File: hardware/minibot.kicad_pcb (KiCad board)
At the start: 2 copper layers, 52 parts, among them J1 USB_OTG, J2 RESET, J3 CONN_01X18, J4 BAUD, J5 SWD, J6 CONN_02X07, SW1 BOOT, SW2 RESET, U1 LSM6DS3US, U2 TLV70233DBV, U3 RN41, U4 STM32F411CEUx, Y1 12MHz

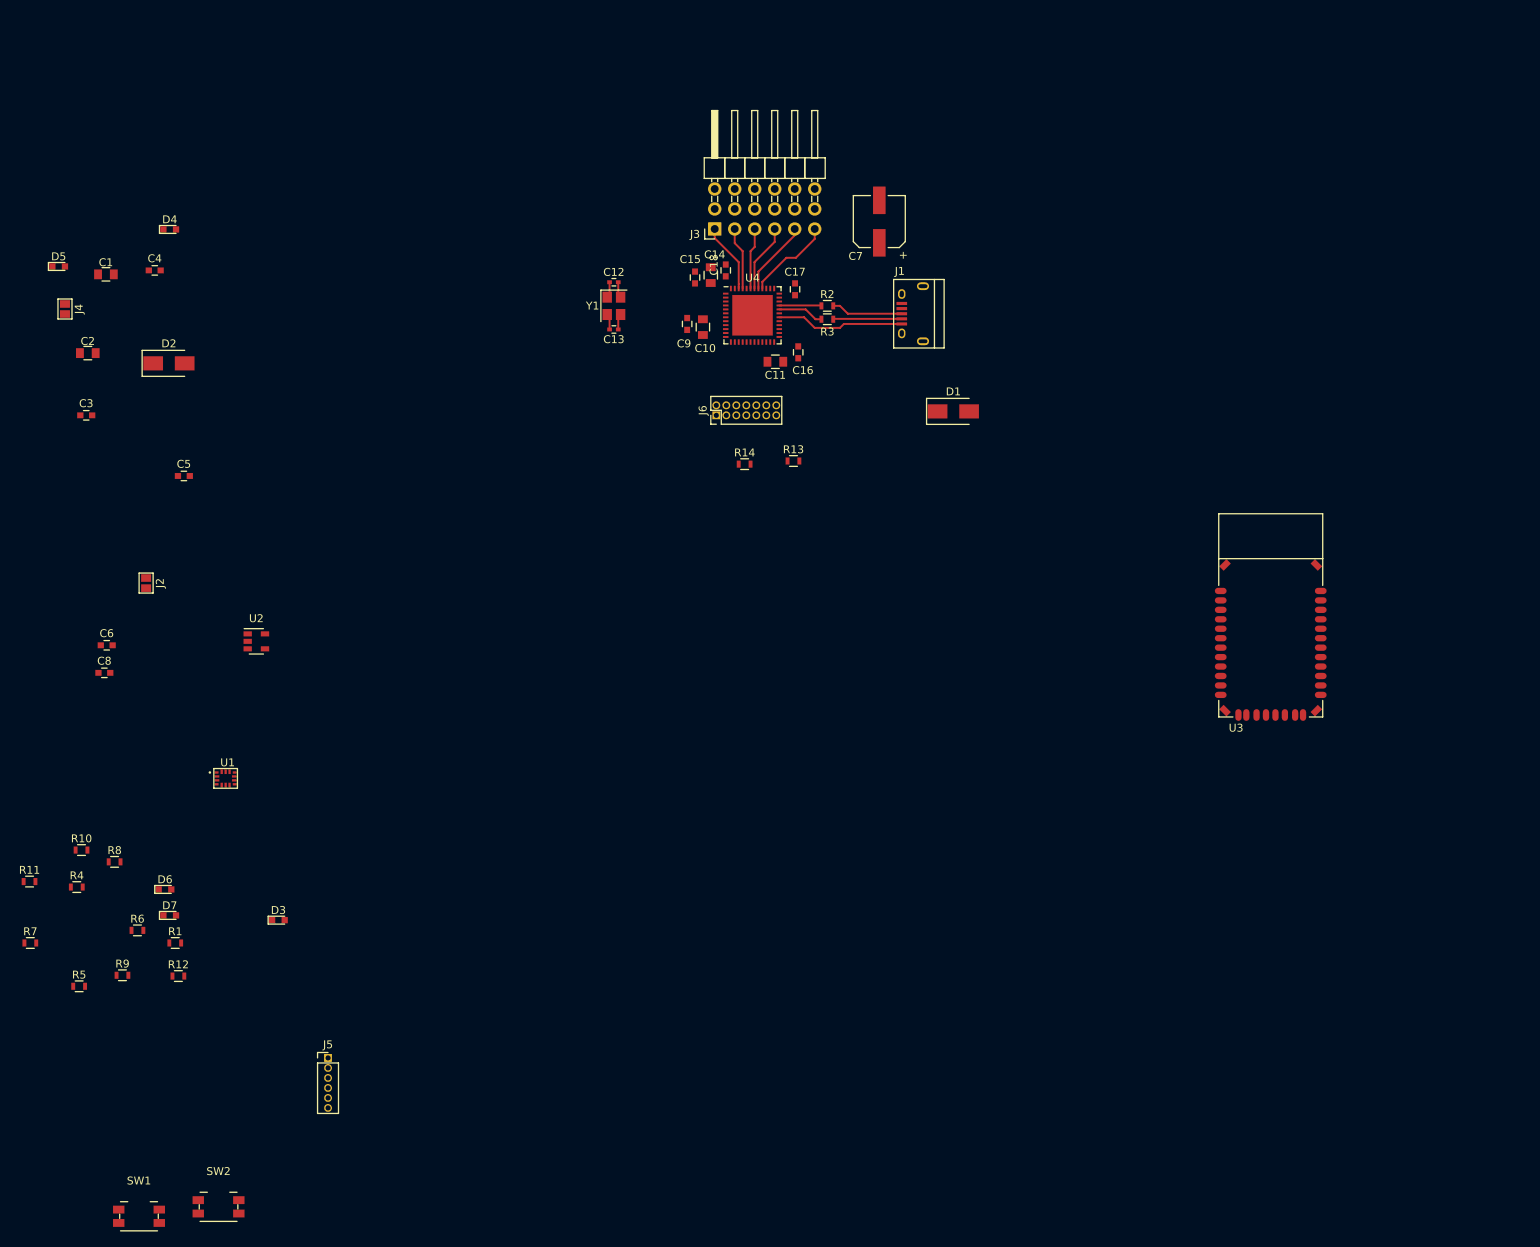
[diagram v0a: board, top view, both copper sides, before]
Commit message: Modify the schematic and PCB. At this stage the pinout should be considered and very careful selection of which peripheral goes where needs to be done.
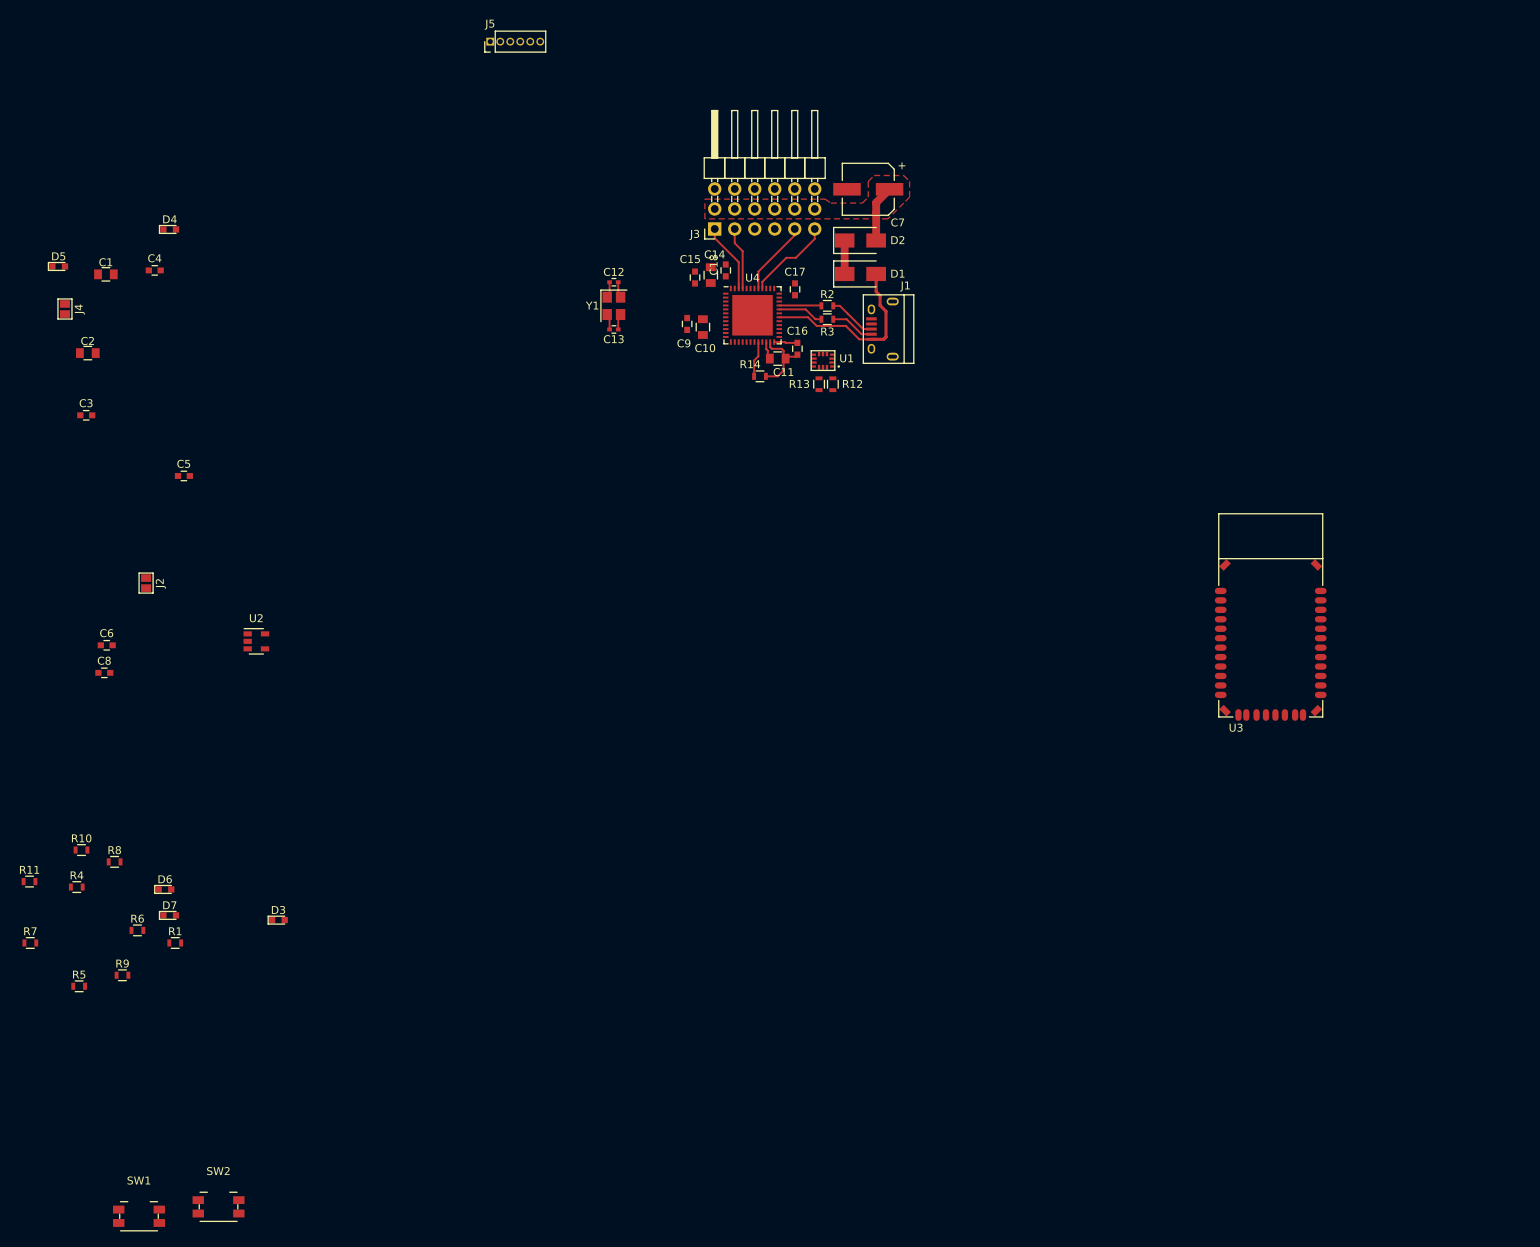
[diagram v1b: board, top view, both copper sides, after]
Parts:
- removed J6: CONN_02X07, Pin_Headers:Pin_Header_Straight_2x07_Pitch1.27mm
- moved J5 130.7 mm to (115.0, 19.8), turned to 90 degrees
- moved R12 112.0 mm to (158.5, 63.2), turned to 270 degrees
- moved U1 92.6 mm to (157.2, 60.2), turned to 180 degrees
- moved D2 89.2 mm to (162.0, 45.0)
- moved D1 21.1 mm to (162.0, 49.2)
- moved R14 11.3 mm to (149.2, 62.2)
- moved R13 10.3 mm to (156.8, 63.2), turned to 270 degrees
- moved C7 4.33 mm to (163.0, 38.5), turned to 180 degrees
- moved J1 4.32 mm to (164.8, 56.2)
- moved C11 0.50 mm to (151.5, 60.0)
- moved C16 0.46 mm to (154.0, 58.8)
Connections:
- C1 pad 2: (no net) -> Net-(C1-Pad2)
- J1 pad 4: (no net) -> Net-(J1-Pad4)
- R12 pad 1: /PB11 -> /PB7
- R13 pad 1: /PB10 -> /PB6
- U1 pad 10: (no net) -> Net-(U1-Pad10)
- U1 pad 13: /PB10 -> /PB6
- U1 pad 14: /PB11 -> /PB7
- U1 pad 4: (no net) -> Net-(U1-Pad4)
- U1 pad 9: (no net) -> Net-(U1-Pad9)
- U3 pad 11: (no net) -> VDD
- U4 pad 18: /PB0 -> /CH2
- U4 pad 19: /PB1 -> /CH3
- U4 pad 25: /PB11 -> /PB12
- U4 pad 26: /PB12 -> /PB13
- U4 pad 27: /PB13 -> /PB14
- U4 pad 28: /PB14 -> /PB15
- U4 pad 29: (no net) -> /PA8
- U4 pad 31: (no net) -> /PA10
- U4 pad 42: /CH2 -> /PB6
- U4 pad 43: /CH3 -> /PB7
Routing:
- net GND: track 4.05 -> 13.9 mm
- net /CH2: track 8.62 -> 0.00 mm
- net /CH3: track 7.78 -> 0.00 mm
- net Net-(C7-Pad1): track 0.00 -> 7.20 mm
- net /PA9: track 16.3 -> 23.4 mm
- net /PB2: track 0.00 -> 4.58 mm
- net +5V: track 0.00 -> 4.25 mm
- net Net-(J1-Pad3): track 9.11 -> 6.07 mm
- net Net-(J1-Pad2): track 8.72 -> 5.71 mm
- net +3V3: track 0.00 -> 2.99 mm
- net Net-(C11-Pad1): track 0.00 -> 2.18 mm
- added copper zone on F.Cu, net Net-(C7-Pad1)

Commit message: Redo the pinout. Plot the PDF. Layout the rest of the board.
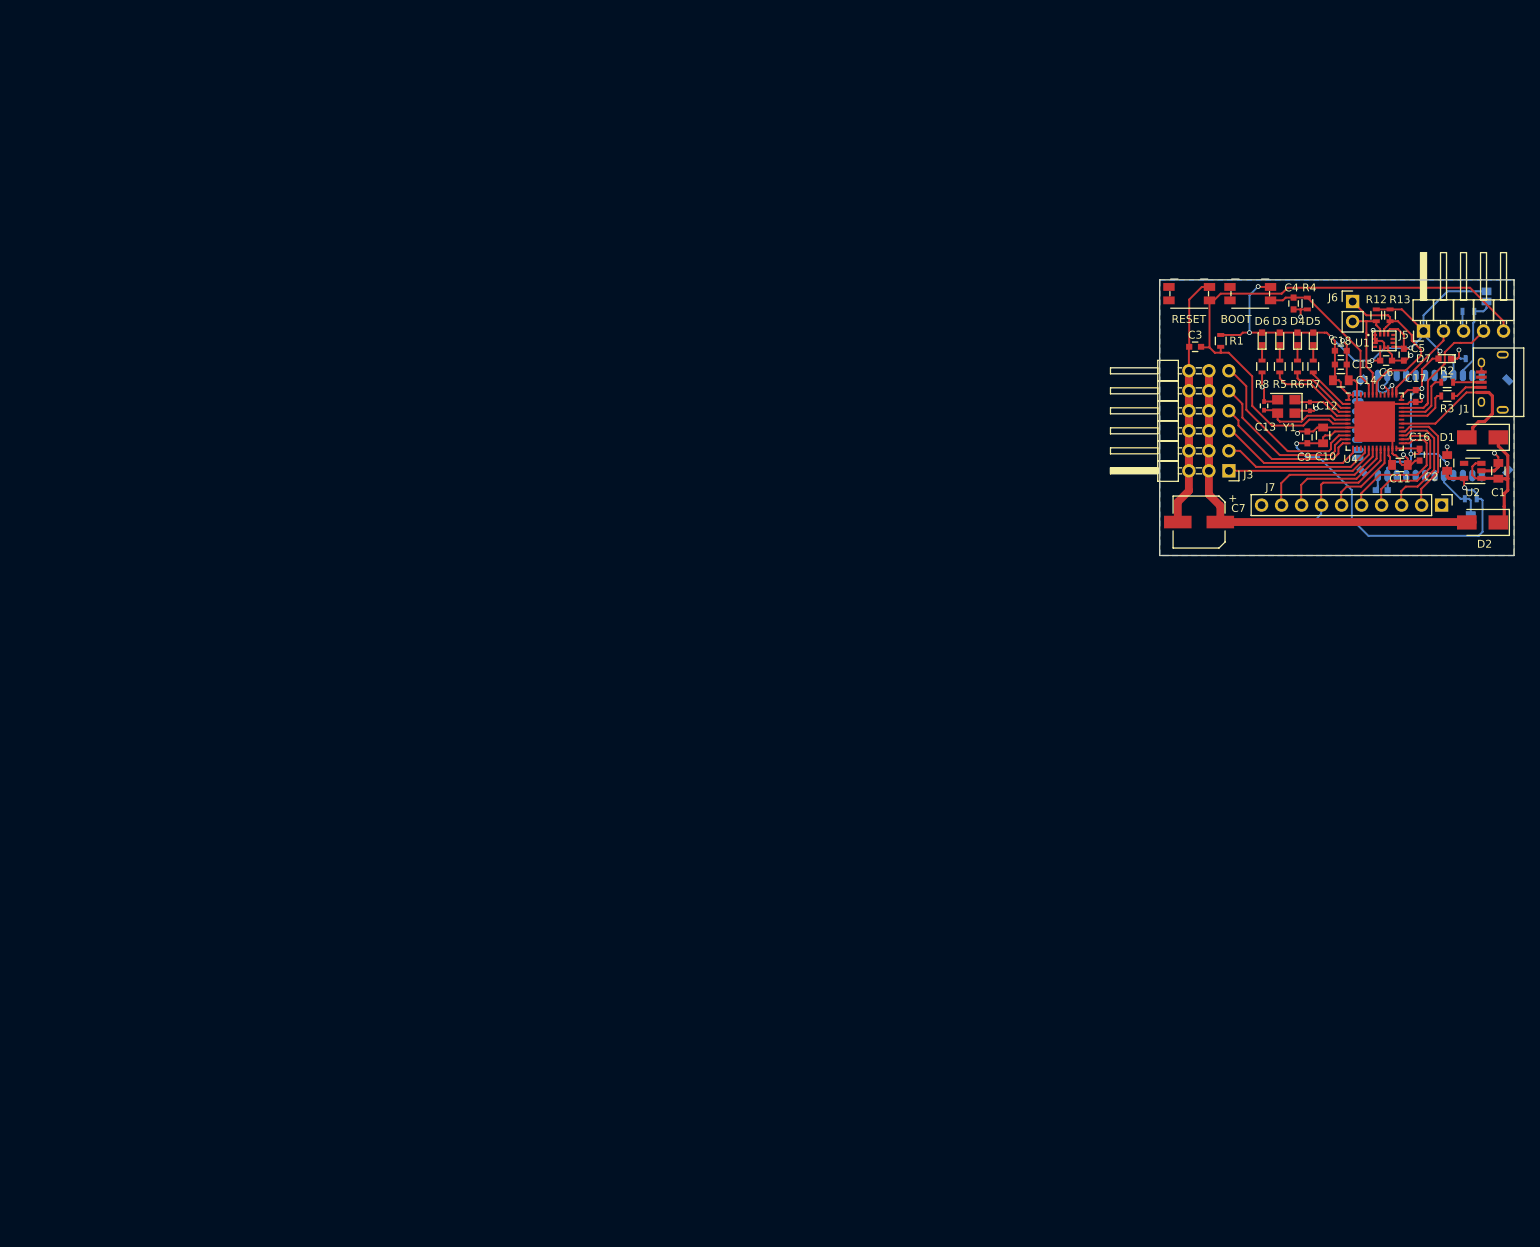
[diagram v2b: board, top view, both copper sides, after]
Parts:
- added J6: CONN_01X02, Pin_Headers:Pin_Header_Straight_1x02_Pitch2.54mm, F.Cu at (224.5, 52.8)
- added J7: CONN_01X10, Pin_Headers:Pin_Header_Straight_1x10_Pitch2.54mm, F.Cu at (235.8, 78.6)
- C8, J2, J4, R10, R11, R14, R9, U3: moved to B.Cu
- J5: value SWD -> CONN_01X05; footprint Pin_Headers:Pin_Header_Straight_1x06_Pitch1.27mm -> Pin_Headers:Pin_Header_Angled_1x05_Pitch2.54mm
- moved R11 196.5 mm to (239.2, 54.0)
- moved R10 185.8 mm to (238.1, 60.0)
- moved SW1 183.4 mm to (211.5, 51.8)
- moved R9 181.6 mm to (239.5, 77.8)
- moved J4 180.5 mm to (241.5, 52.1)
- moved R7 178.6 mm to (219.5, 61.0), turned to 90 degrees
- moved C1 178.6 mm to (243.0, 74.2), turned to 270 degrees
- moved D7 176.7 mm to (236.2, 60.0), turned to 180 degrees
- moved C2 173.2 mm to (236.5, 73.2), turned to 270 degrees
- moved R4 172.9 mm to (218.8, 53.0), turned to 270 degrees
- moved R5 171.6 mm to (215.2, 61.0), turned to 90 degrees
- moved SW2 169.2 mm to (203.8, 51.8)
- moved J2 168.4 mm to (239.5, 80.5), turned to 180 degrees
- moved C6 166.4 mm to (228.8, 60.2)
- moved C8 163.9 mm to (228.2, 76.7), turned to 180 degrees
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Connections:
- C1 pad 2: Net-(C1-Pad2) -> +5V
- SW2 pad 1: /nRST -> GND
- SW2 pad 2: GND -> /nRST
- U3 pad : (no net) -> GND
- U3 pad 11: VDD -> +3V3
- U3 pad 15: /BT_CTS -> Net-(U3-Pad15)
- U3 pad 16: /BT_RTS -> GND
- U4 pad 10: /BT_CTS -> /CH0
- U4 pad 11: /BT_RTS -> /CH1
- U4 pad 12: /BT_TXD -> /CH2
- U4 pad 13: /BT_RXD -> /CH3
- U4 pad 16: /PA6 -> /CH4
- U4 pad 17: /PA7 -> /CH5
- U4 pad 18: /CH2 -> /PB0
- U4 pad 19: /CH3 -> /PB1
- U4 pad 38: /PA15 -> /BT_TXD
- U4 pad 39: /PB3 -> /BT_RXD
- U4 pad 40: /CH0 -> /PB4
- U4 pad 41: /CH1 -> /PB5
- U4 pad 45: /CH4 -> /PB8
- U4 pad 46: /CH5 -> /PB9
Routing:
- net +3V3: track 2.99 -> 165.6 mm, vias 0 -> 11
- net GND: track 13.9 -> 150.8 mm, vias 0 -> 11
- net /nRST: track 0.00 -> 73.2 mm
- net Net-(C7-Pad1): track 7.20 -> 64.6 mm
- net /PB6: track 0.00 -> 23.3 mm
- net /BOOT: track 0.00 -> 20.4 mm
- net /CH2: track 0.00 -> 19.3 mm
- net /CH3: track 0.00 -> 18.5 mm
- net /PA13: track 0.00 -> 17.1 mm
- net /PB12: track 0.00 -> 17.0 mm
- net /PB13: track 0.00 -> 16.3 mm
- net /PB0: track 0.00 -> 16.2 mm
- net /PB14: track 0.00 -> 15.3 mm
- net /PB7: track 0.00 -> 14.6 mm
- net +5V: track 4.25 -> 18.7 mm
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- added copper zone on B.Cu, net GND
- removed copper zone on F.Cu, net Net-(C7-Pad1)
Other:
- board outline added: 45 x 35 mm
- net class Default: clearance 0.2 -> 0.15
- rule trace_clearance: 0.2 -> 0.15
- board text added: "BAUD"
- board text added: "BOOT"
- board text added: "RESET"

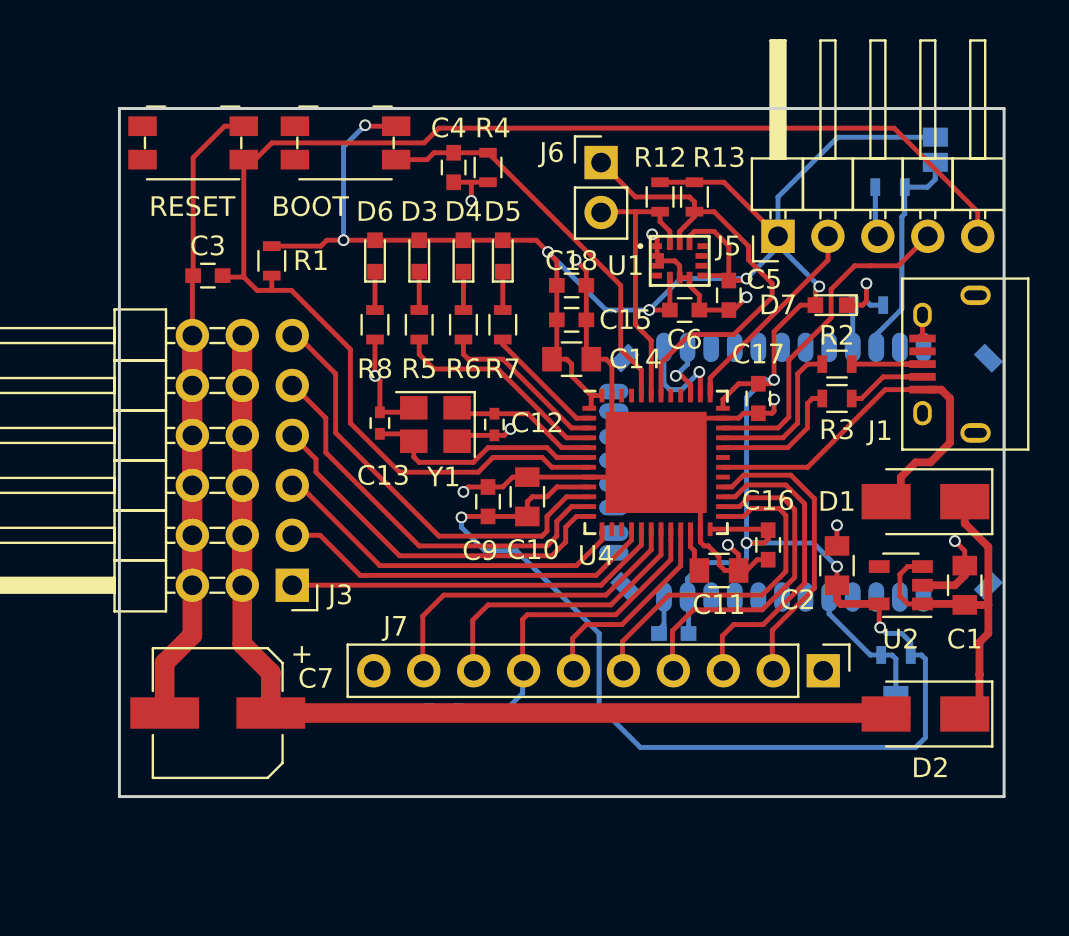
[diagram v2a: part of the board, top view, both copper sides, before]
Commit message: Tweak the layout a little bit. Add mounting holes and some pads to solder the power leads onto.
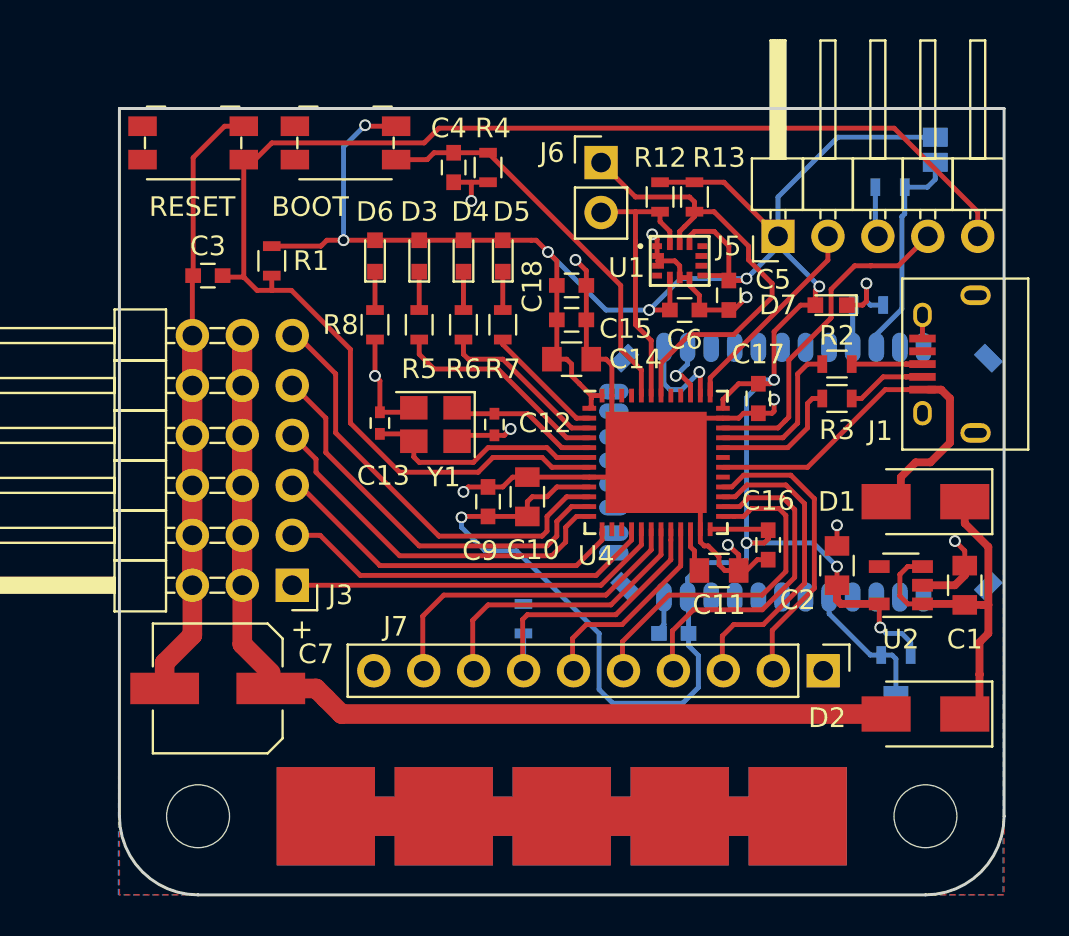
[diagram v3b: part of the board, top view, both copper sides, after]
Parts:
- added J10: CONN_01X01, parts:Pad, F.Cu at (222.5, 86.0)
- added J11: CONN_01X01, parts:Pad, F.Cu at (228.5, 86.0)
- added J12: CONN_01X01, parts:Pad, F.Cu at (234.5, 86.0)
- added J13: CONN_01X01, parts:Pad, B.Cu at (228.5, 86.0)
- added J14: CONN_01X01, parts:Pad, B.Cu at (222.5, 86.0)
- added J15: CONN_01X01, parts:Pad, B.Cu at (216.5, 86.0)
- added J16: CONN_01X01, parts:Pad, B.Cu at (210.5, 86.0)
- added J17: CONN_01X01, parts:Pad, B.Cu at (234.5, 86.0)
- added J8: CONN_01X01, parts:Pad, F.Cu at (210.5, 86.0)
- added J9: CONN_01X01, parts:Pad, F.Cu at (216.5, 86.0)
- added REF**: MountingHole_3.2mm_M3, Mounting_Holes:MountingHole_3.2mm_M3, F.Cu at (241.0, 86.0)
- added REF**: MountingHole_3.2mm_M3, Mounting_Holes:MountingHole_3.2mm_M3, F.Cu at (204.0, 86.0)
- moved R14 6.24 mm to (220.6, 76.0), turned to 90 degrees
- moved C7 1.25 mm to (205.0, 79.5)
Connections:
- U3 pad : GND -> (no net)
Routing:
- net Net-(J13-Pad1): track 0.00 -> 24.0 mm
- net Net-(J10-Pad1): track 0.00 -> 24.0 mm
- net +3V3: track 165.6 -> 150.8 mm
- net /PB2: track 17.8 -> 14.3 mm
- net Net-(C7-Pad1): track 64.6 -> 62.3 mm
- net GND: track 150.8 -> 149.6 mm
- added copper zone on F.Cu, net GND
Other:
- board size 45 x 35 mm -> 45 x 40 mm
